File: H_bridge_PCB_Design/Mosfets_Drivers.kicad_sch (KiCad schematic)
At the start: 44 parts, among them J2 TMS-102-21-G-S, J3 TMS-102-21-G-S, Q1 IRLB4030PBF, Q10 IPD90N10S4L06ATMA1, Q2 IRLB4030PBF, Q3 IRLB4030PBF, Q4 IRLB4030PBF, Q5 IPD90N10S4L06ATMA1, Q6 IPD90N10S4L06ATMA1, Q9 IPD90N10S4L06ATMA1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

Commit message: Updated PCB design files
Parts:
- removed C13: MKP1847H55025JK2, SamacSys_Parts:MKP1847H55025JK2, symbol SamacSys_Parts:MKP1847H55025JK2
- added C13, C16, C22: MKS4C042204C00KSSD, SamacSys_Parts:MKS4C042204C00KSSD, symbol SamacSys_Parts:MKS4C042204C00KSSD
- added J10, J11, J6, J7, J8, J9: TMS-102-21-G-S, SamacSys_Parts:TMS-102-YY-XX-S, symbol SamacSys_Parts:TMS-102-21-G-S
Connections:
- net Out- renamed Cout-
- net Cout-: now also J10.2
- net SV2 renamed Cout+
- net Cout+: now also J11.1
- new net: C13.1, J7.1, J9.2
- new net: C16.1, J10.1, J7.2
- new net: C22.1, J9.1
- new net: C22.2, J8.2
- new net: C16.2, J11.2, J6.1
- new net: C13.2, J6.2, J8.1
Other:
- moved on the sheet: D1, D2, D3, D5

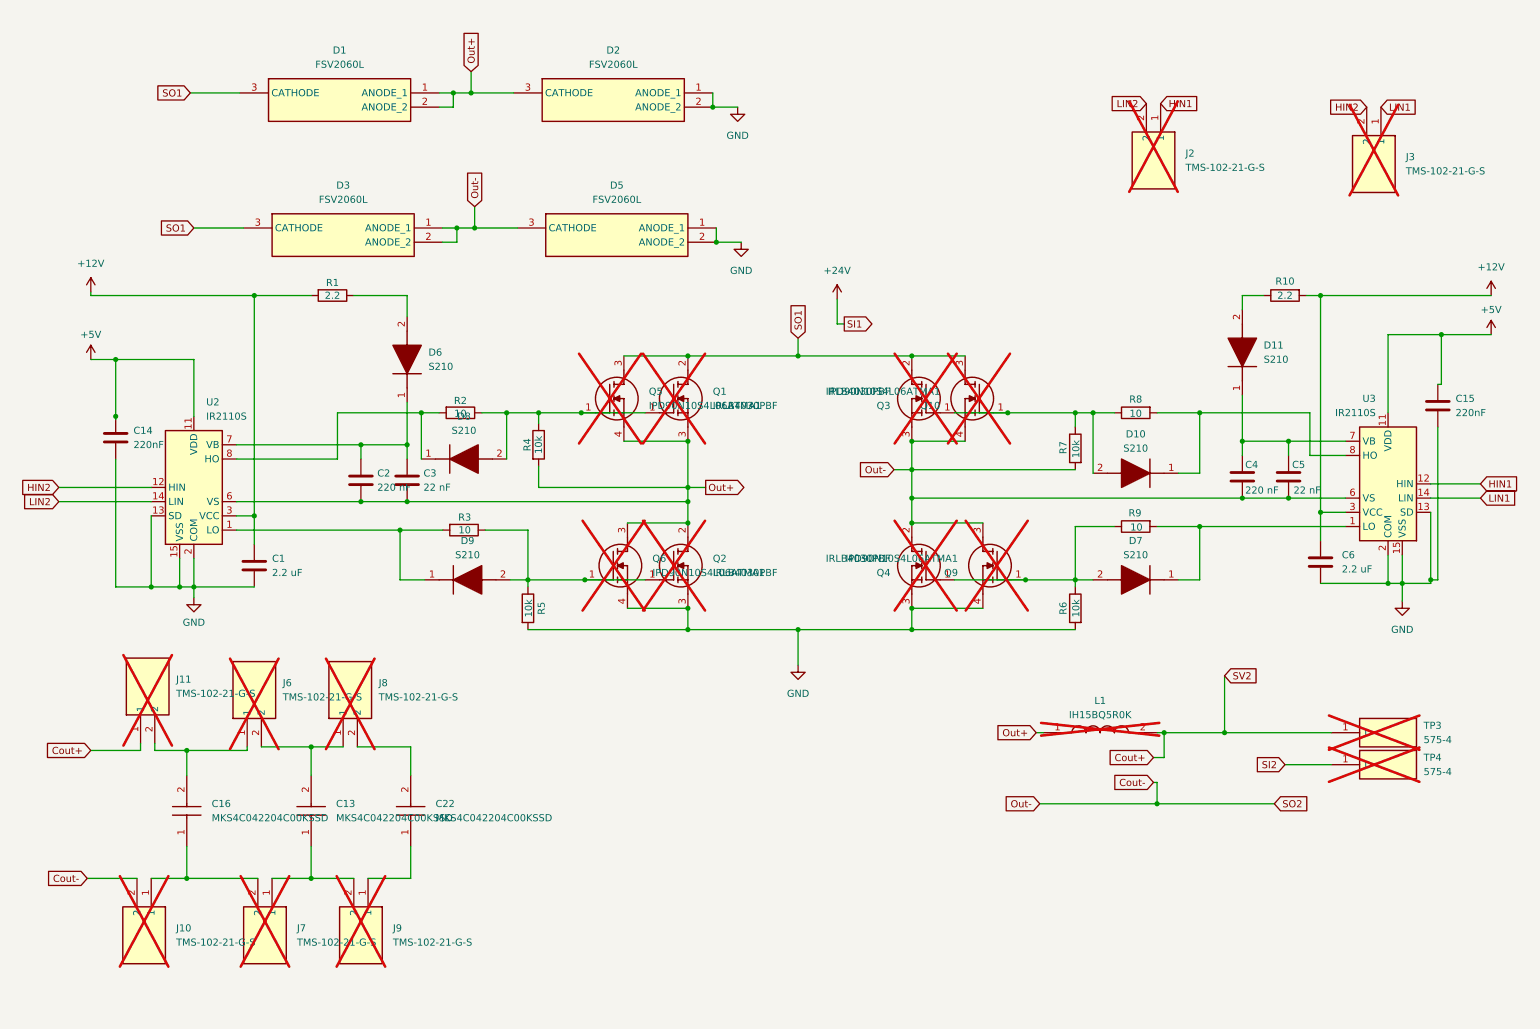
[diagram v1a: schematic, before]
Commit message: Interrupt for PWM and unipolar modulation
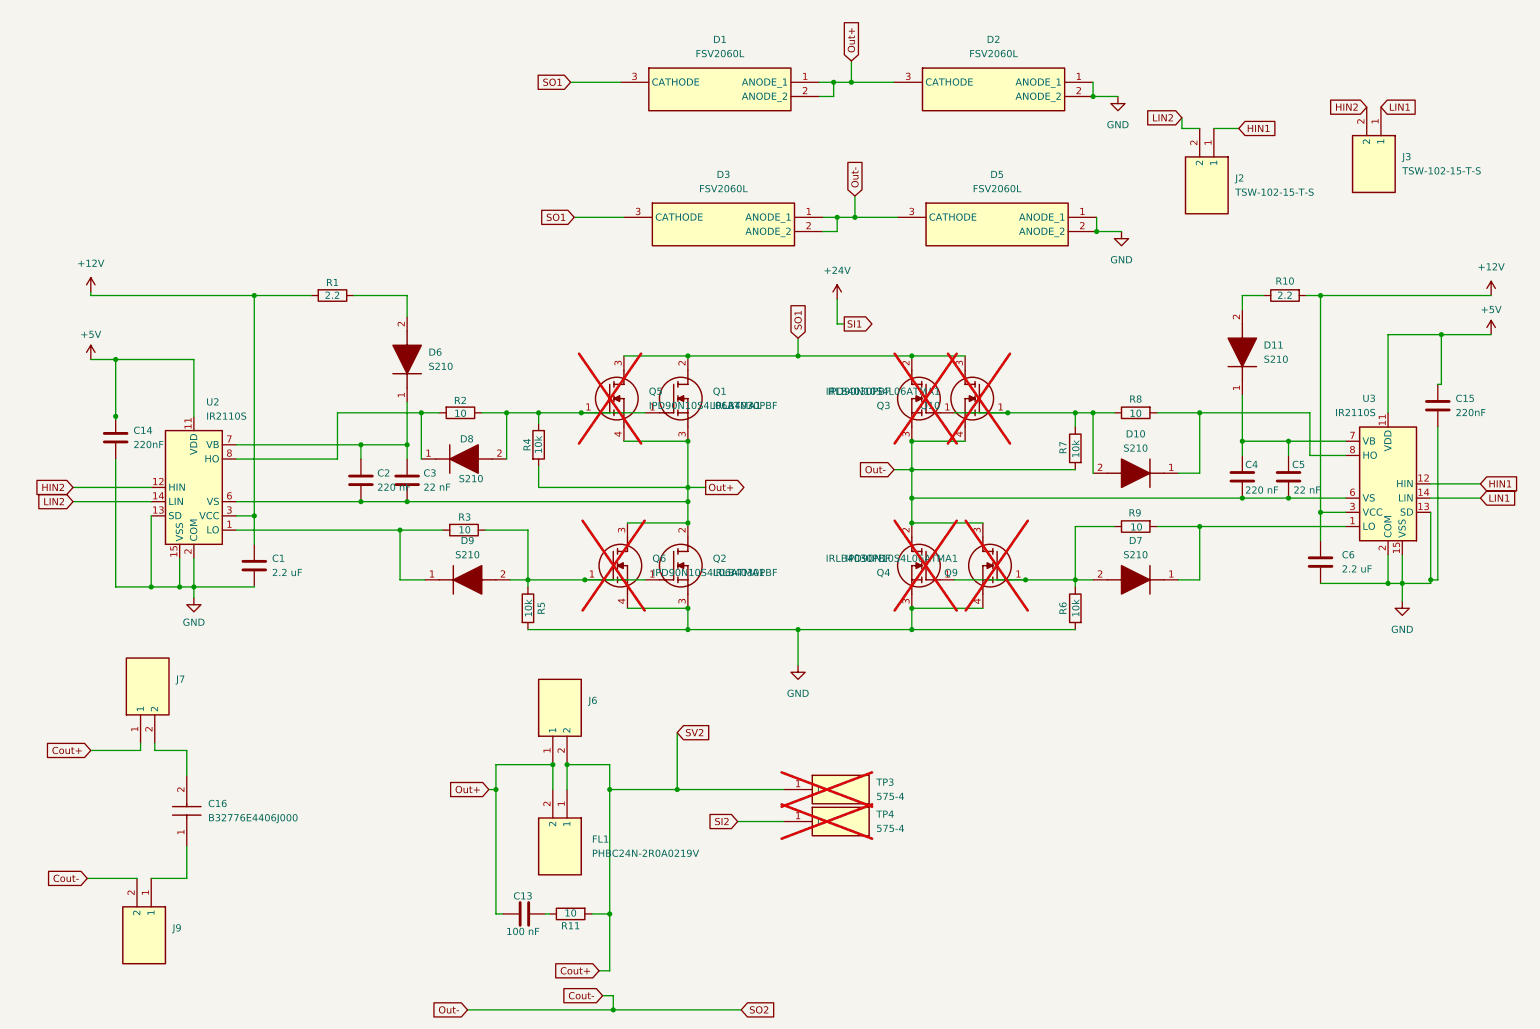
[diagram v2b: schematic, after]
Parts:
- removed C13, C16, C22: MKS4C042204C00KSSD, SamacSys_Parts:MKS4C042204C00KSSD, symbol SamacSys_Parts:MKS4C042204C00KSSD
- removed J10, J11, J2, J3, J6, J7, J8, J9: TMS-102-21-G-S, SamacSys_Parts:TMS-102-YY-XX-S, symbol SamacSys_Parts:TMS-102-21-G-S
- removed L1: IH15BQ5R0K, SamacSys_Parts:IH15BQ5R0K, symbol SamacSys_Parts:IH15BQ5R0K
- added C13: 100 nF, Resistor_SMD:R_0805_2012Metric_Pad1.20x1.40mm_HandSolder, symbol Device:C
- added C16: B32776E4406J000, SamacSys_Parts:B32776E4406J000, symbol SamacSys_Parts:B32776E4406J000
- added FL1: PHBC24N-2R0A0219V, SamacSys_Parts:PHBC24N2R0A0219V, symbol SamacSys_Parts:PHBC24N-2R0A0219V
- added J2, J3, J6, J7, J9: TSW-102-15-T-S, SamacSys_Parts:TSW-102-XX-YY-S, symbol SamacSys_Parts:TSW-102-15-T-S
- added R11: 10, Resistor_SMD:R_0805_2012Metric_Pad1.20x1.40mm_HandSolder, symbol Device:R
- Q1, Q2: now fitted
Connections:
- net Cout+: now also FL1.1, J6.2, J7.1, R11.2
- net Cout-: now also J9.2
- net HIN1: now also J2.1
- net HIN2: now also J3.2
- net LIN1: now also J3.1
- net LIN2: now also J2.2
- net Out+: now also C13.2, FL1.2, J6.1
- new net: C16.1, J9.1
- new net: C16.2, J7.2
- new net: C13.1, R11.1
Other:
- moved on the sheet: D1, D2, D3, D5, TP3, TP4

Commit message: huge changes output measurement
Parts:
- removed J6: TSW-102-15-T-S, SamacSys_Parts:TSW-102-XX-YY-S, symbol SamacSys_Parts:TSW-102-15-T-S
- removed R11: 10, Resistor_SMD:R_0805_2012Metric_Pad1.20x1.40mm_HandSolder, symbol Device:R
- added C28, C29: 1 uF, Resistor_SMD:R_0805_2012Metric_Pad1.20x1.40mm_HandSolder, symbol Device:C
- added C30: 100 nF, Resistor_SMD:R_0805_2012Metric_Pad1.20x1.40mm_HandSolder, symbol Device:C
- C13: LCSC Part# C354366 -> C513763
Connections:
- net GND: now also C13.2, C28.2, C29.2, C30.2
- net Out+: no longer C13.2
- net SO1: now also C13.1, C28.1, C29.1, C30.1

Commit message: new pcb
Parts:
- added R20: 0, Resistor_SMD:R_0805_2012Metric_Pad1.20x1.40mm_HandSolder, symbol Device:R
- C1, C6: LCSC Part # (none) -> C513763; LCSC Part# C513763 -> (none)
- C13, C30: LCSC Part # (none) -> C49678; LCSC Part# C513763 -> (none)
- C14, C15, C2, C4: LCSC Part # (none) -> C354366; LCSC Part# C354366 -> (none)
- C28, C29: LCSC Part # (none) -> C28323; LCSC Part# C513763 -> (none)
- C3, C5: LCSC Part # (none) -> C2181592; LCSC Part# C2181592 -> (none)
- D1, D2, D3, D5: LCSC Part # (none) -> C110669; LCSC Part# C110669 -> (none)
- D10, D11, D6, D7, D8, D9: LCSC Part # (none) -> C184977; LCSC Part# C184977 -> (none)
- Q1, Q2: LCSC Part # (none) -> C2663
- Q3, Q4: LCSC Part # (none) -> C2663; now fitted
- R1, R10: LCSC Part # (none) -> C25301; LCSC Part# C25301 -> (none)
- R2, R3, R8, R9: LCSC Part # (none) -> C3016584; LCSC Part# C3016584 -> (none)
- R4, R5, R6, R7: LCSC Part # (none) -> C84376; LCSC Part# C84376 -> (none)
- U2, U3: LCSC Part # (none) -> C2968; LCSC Part# C2968 -> (none)
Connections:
- net GND: now also R20.1; no longer U2.13 (SD), U3.13 (SD)
- new net Shutoff: R20.2, U2.13 (SD), U3.13 (SD)
